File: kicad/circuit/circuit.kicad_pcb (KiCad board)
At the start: 2 copper layers, 68.6 x 53.4 mm, 14 parts, among them J1.1 Digital, J1.2 Analog, J2 Handbrake, J3 Encoder, J4 Joystick, J5 Pedals, J6 RJ45, J7.1.1 LCD Socket, J7.1.2 PCF8574 LCD Socekt, J7.2 PCF8574 I²C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

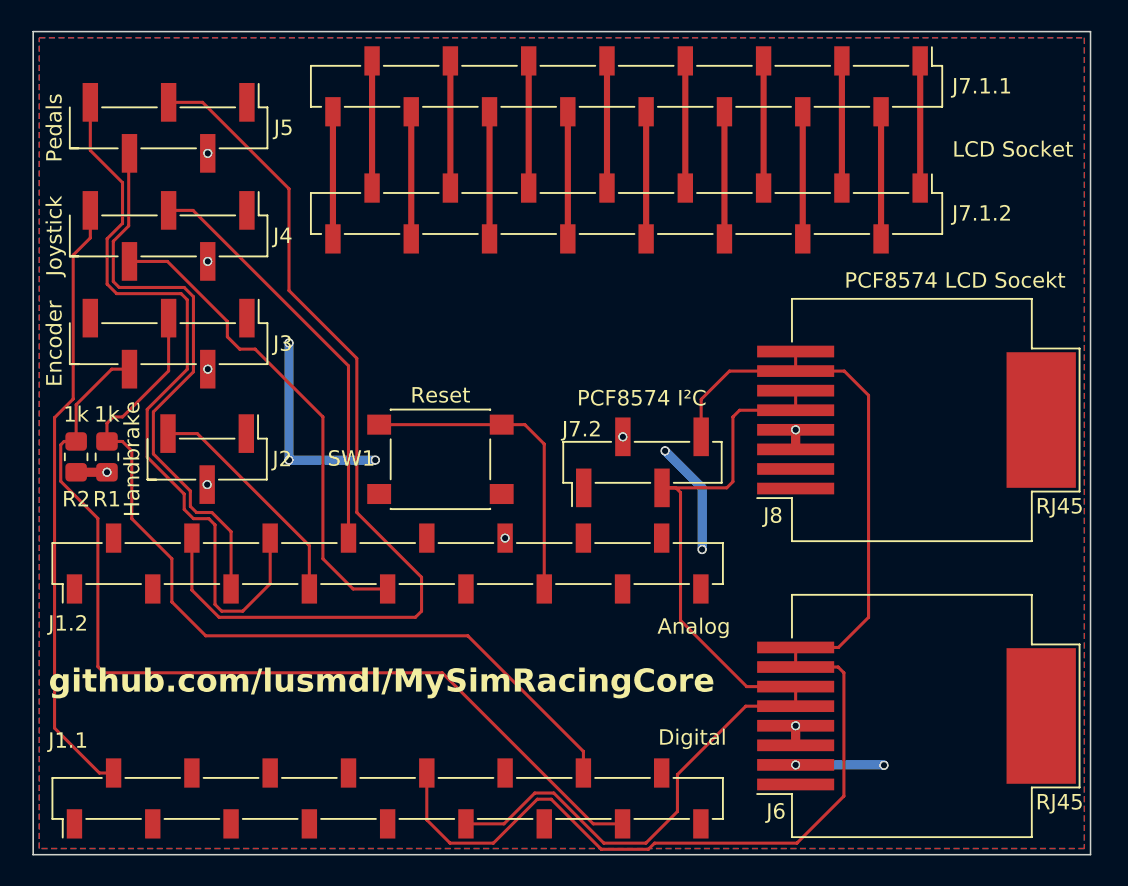
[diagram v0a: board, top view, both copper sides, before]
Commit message: remove lcd and add gitignore for kicad
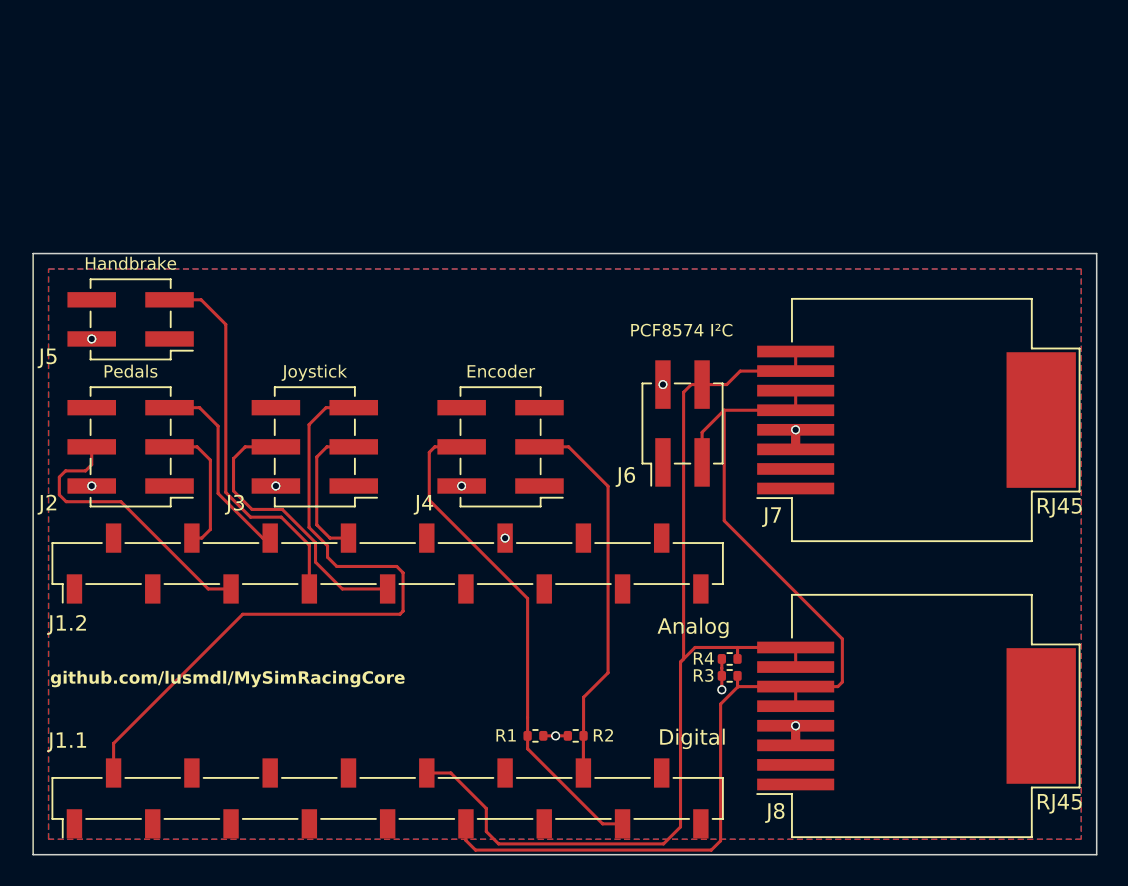
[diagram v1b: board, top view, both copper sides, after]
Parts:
- removed the J2 at (111.3, 74.3)
- removed J7.1.1: LCD Socket, Connector_PinSocket_2.54mm:PinSocket_1x16_P2.54mm_Vertical_SMD_Pin1Left
- removed J7.1.2: PCF8574 LCD Socekt, Connector_PinSocket_2.54mm:PinSocket_1x16_P2.54mm_Vertical_SMD_Pin1Left
- removed SW1: Reset, Button_Switch_SMD:SW_Push_1P1T_NO_6x6mm_H9.5mm
- added J5: Handbrake, Connector_PinHeader_2.54mm:PinHeader_2x02_P2.54mm_Vertical_SMD, F.Cu at (106.3, 65.3)
- added R3: 4.7k, Resistor_SMD:R_0402_1005Metric, F.Cu at (145.2, 88.4)
- added R4: 4.7k, Resistor_SMD:R_0402_1005Metric, F.Cu at (145.2, 87.3)
- J2: renamed from J5; footprint Connector_PinHeader_2.54mm:PinHeader_1x05_P2.54mm_Vertical_SMD_Pin1Left -> Connector_PinHeader_2.54mm:PinHeader_2x03_P2.54mm_Vertical_SMD
- J3: renamed from J4; footprint Connector_PinHeader_2.54mm:PinHeader_1x05_P2.54mm_Vertical_SMD_Pin1Left -> Connector_PinHeader_2.54mm:PinHeader_2x03_P2.54mm_Vertical_SMD
- J4: renamed from J3; footprint Connector_PinHeader_2.54mm:PinHeader_1x05_P2.54mm_Vertical_SMD_Pin1Left -> Connector_PinHeader_2.54mm:PinHeader_2x03_P2.54mm_Vertical_SMD
- J6: renamed from J7.2; footprint Connector_PinHeader_2.54mm:PinHeader_1x04_P2.54mm_Vertical_SMD_Pin1Left -> Connector_PinHeader_2.54mm:PinHeader_2x02_P2.54mm_Vertical_SMD
- R1, R2: footprint Resistor_SMD:R_0805_2012Metric_Pad1.20x1.40mm_HandSolder -> Resistor_SMD:R_0402_1005Metric
- moved R2 37.1 mm to (135.2, 92.3), turned to 0 degrees
- moved R1 33.2 mm to (132.6, 92.3), turned to 180 degrees
- moved J4 22.6 mm to (130.3, 73.5), turned to 180 degrees
- moved J2 20.8 mm to (106.3, 73.5), turned to 180 degrees
- moved J3 16.7 mm to (118.3, 73.5), turned to 180 degrees
- moved J6 3.62 mm to (142.1, 72.0)
- renumbered J8 to J7, J6 to J8
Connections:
- R1 pad 2: /A -> /B
- R2 pad 2: /B -> /A
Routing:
- net /A0: track 60.3 -> 8.94 mm
- net /A2: track 49.4 -> 12.6 mm
- net /A: track 54.9 -> 24.8 mm
- net /B: track 61.5 -> 32.3 mm
- net GND: track 26.3 -> 0.00 mm, vias 7 -> 0
- net /~{RESET}: track 20.6 -> 0.00 mm
- net /A1: track 37.1 -> 18.4 mm
- net /A4: track 27.0 -> 9.49 mm
- net /*D3/SCL: track 83.1 -> 67.0 mm
- net /A5: track 31.5 -> 18.5 mm
- net /A3: track 15.0 -> 24.9 mm
- net Net-(J7.1.1-Pin_9): track 8.25 -> 0.00 mm
- net Net-(J7.1.1-Pin_8): track 8.25 -> 0.00 mm
- net Net-(J7.1.1-Pin_7): track 8.25 -> 0.00 mm
- net Net-(J7.1.1-Pin_6): track 8.25 -> 0.00 mm
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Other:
- board size 68.6 x 53.4 mm -> 69 x 39 mm

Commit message: add ps4 joystick pcb + data over rj45
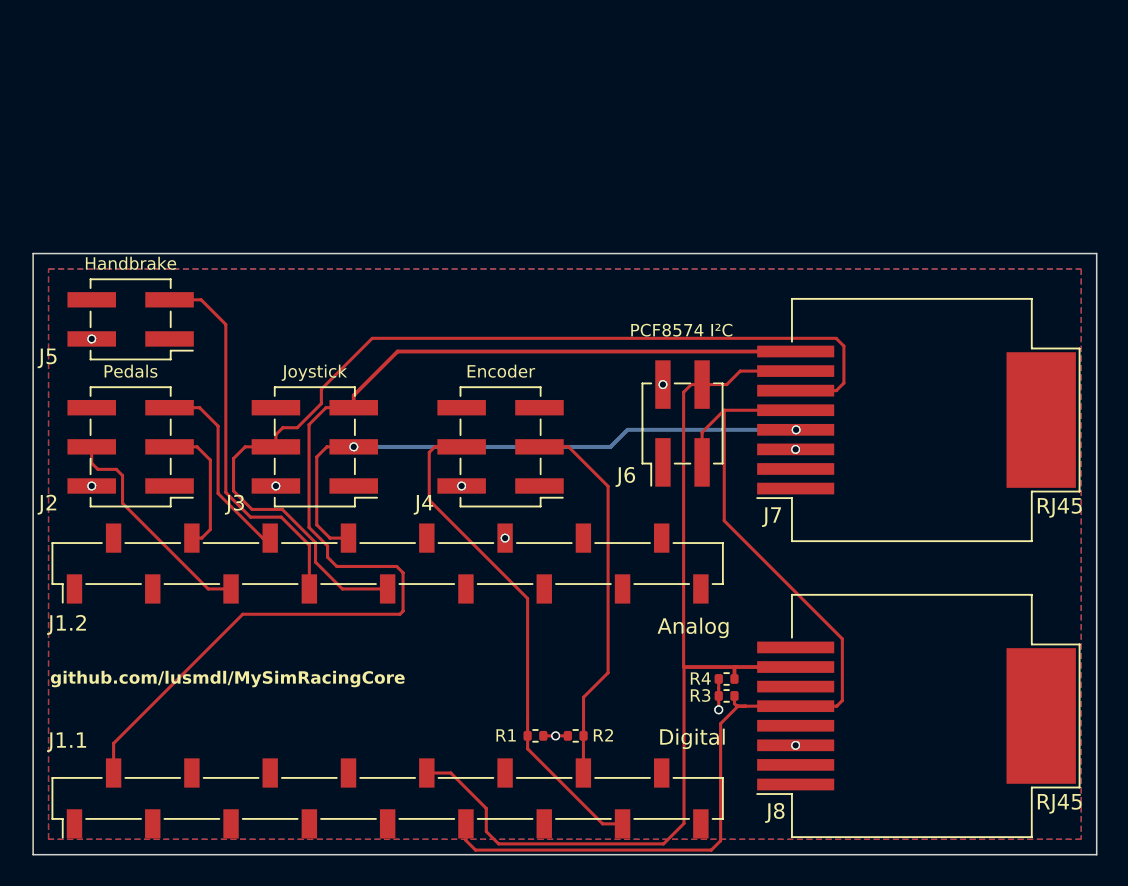
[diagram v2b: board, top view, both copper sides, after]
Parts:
- moved R3 1.32 mm to (145.0, 89.7)
- moved R4 1.32 mm to (145.0, 88.6)
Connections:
- J7 pad 4: +5V -> /A4
- J7 pad 6: /D2/SDA -> /A5
- J7 pad 8: /*D3/SCL -> /*D11
- J8 pad 4: +5V -> unconnected-(J8-Pad4)
- J8 pad 6: /D2/SDA -> unconnected-(J8-Pad6)
- J8 pad 8: /*D3/SCL -> unconnected-(J8-Pad8)
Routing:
- net /A5: track 18.5 -> 65.3 mm
- net /A4: track 9.49 -> 40.8 mm, vias 0 -> 2
- net /*D11: track 44.5 -> 75.2 mm
- net /A1: track 18.4 -> 14.5 mm
- net /*D3/SCL: track 67.0 -> 63.9 mm
- net +5V: track 6.13 -> 3.59 mm
- net /D2/SDA: track 68.1 -> 66.2 mm

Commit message: add force feedback device to layout
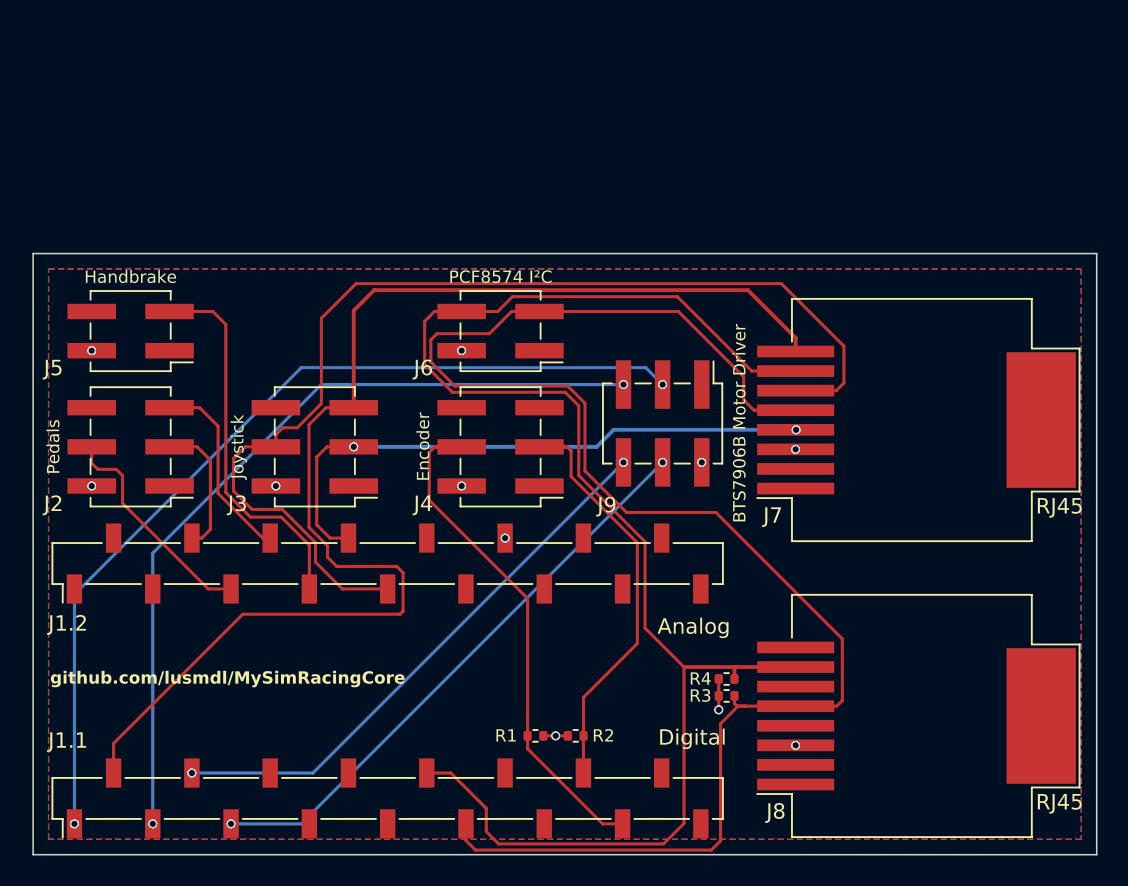
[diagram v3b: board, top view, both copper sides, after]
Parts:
- added J9: BTS7906B Motor Driver, Connector_PinHeader_2.54mm:PinHeader_2x03_P2.54mm_Vertical_SMD, F.Cu at (140.8, 72.0)
- moved J6 13.2 mm to (130.3, 66.0), turned to 180 degrees
- moved J5 0.76 mm to (106.3, 66.0)
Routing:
- net /D12: track 0.00 -> 59.6 mm, vias 0 -> 2
- net /*D10: track 0.00 -> 52.6 mm, vias 0 -> 2
- net /D2/SDA: track 66.2 -> 105.6 mm
- net /D8: track 0.00 -> 37.7 mm, vias 0 -> 2
- net /*D9: track 0.00 -> 36.3 mm, vias 0 -> 2
- net /*D3/SCL: track 63.9 -> 98.6 mm
- net /*D11: track 75.2 -> 82.2 mm
- net /A5: track 65.3 -> 70.9 mm
- net /A: track 24.8 -> 26.3 mm
- net +5V: vias 10 -> 11
